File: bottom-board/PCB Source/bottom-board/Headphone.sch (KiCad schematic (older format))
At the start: 29 parts, among them P14 AudioJack3, Q10 MMBFJ110, Q9 MMBFJ110, U8 LM4811

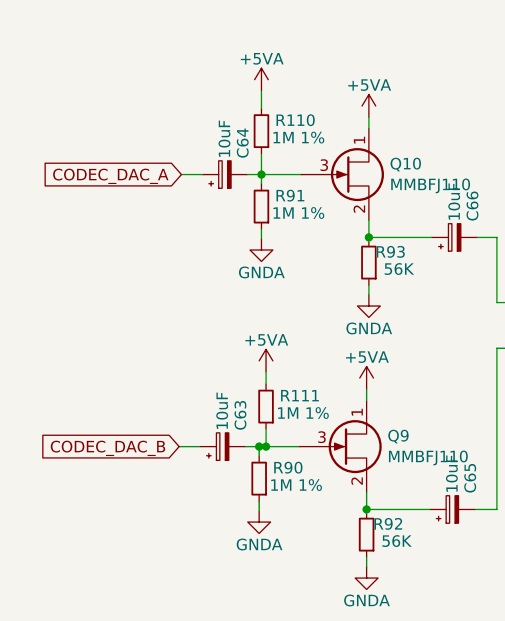
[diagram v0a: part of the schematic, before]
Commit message: update PCB, add noisefix components
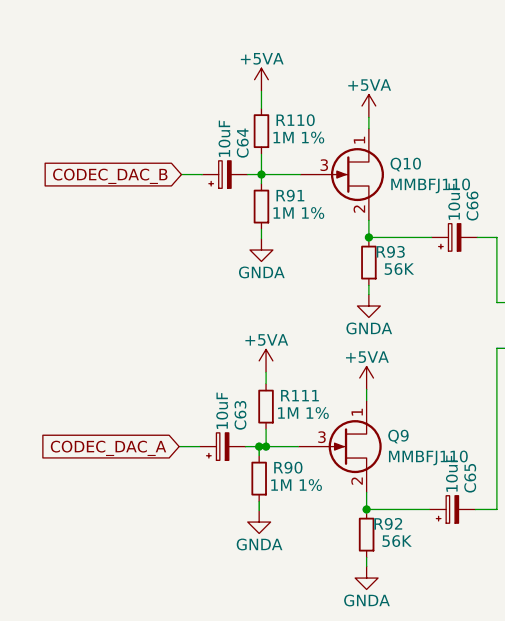
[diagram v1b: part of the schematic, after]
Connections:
- net CODEC_DAC_A: now also C63.1; no longer C64.1
- net CODEC_DAC_B: now also C64.1; no longer C63.1
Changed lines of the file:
@@
 Wire Wire Line
 	3965 2775 3965 2825
+Text GLabel 3145 3025 0    50   Input ~ 0
+CODEC_DAC_B
 Text GLabel 3135 4215 0    50   Input ~ 0
-CODEC_DAC_B
-Text GLabel 3145 3025 0    50   Input ~ 0
 CODEC_DAC_A
 Wire Wire Line

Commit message: update fabrication data
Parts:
- C67, C69: footprint Capacitor_SMD:C_0603_1608Metric -> Capacitor_SMD:C_0805_2012Metric; MPN EMK107BBJ106MA-T -> GRM219R61E106KA12D
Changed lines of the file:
@@
 F 0 "C67" H 6095 3080 50  0000 R CNN
 F 1 "10uF" H 5920 2930 50  0000 L CNN
-F 2 "Capacitor_SMD:C_0603_1608Metric" H 6135 3010 60  0001 C CNN
+F 2 "Capacitor_SMD:C_0805_2012Metric" H 6135 3010 60  0001 C CNN
 F 3 "" H 6135 3010 60  0000 C CNN
-F 4 "EMK107BBJ106MA-T" H 1685 1310 50  0001 C CNN "MPN"
+F 4 "GRM219R61E106KA12D" H 1685 1310 50  0001 C CNN "MPN"
 	1    6135 3010
 	1    0    0    -1
@@
 F 0 "C69" H 6255 4280 50  0000 R CNN
 F 1 "10uF" H 6080 4130 50  0000 L CNN
-F 2 "Capacitor_SMD:C_0603_1608Metric" H 6295 4210 60  0001 C CNN
+F 2 "Capacitor_SMD:C_0805_2012Metric" H 6295 4210 60  0001 C CNN
 F 3 "" H 6295 4210 60  0000 C CNN
-F 4 "EMK107BBJ106MA-T" H 1845 2510 50  0001 C CNN "MPN"
+F 4 "GRM219R61E106KA12D" H 1845 2510 50  0001 C CNN "MPN"
 	1    6295 4210
 	1    0    0    -1

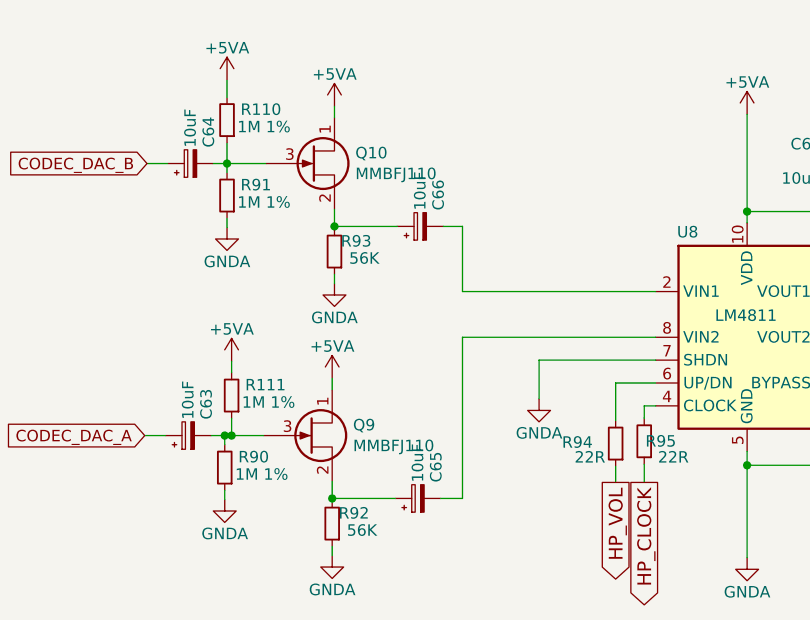
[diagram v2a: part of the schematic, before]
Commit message: change input bias 5->6V, reduce harmonics
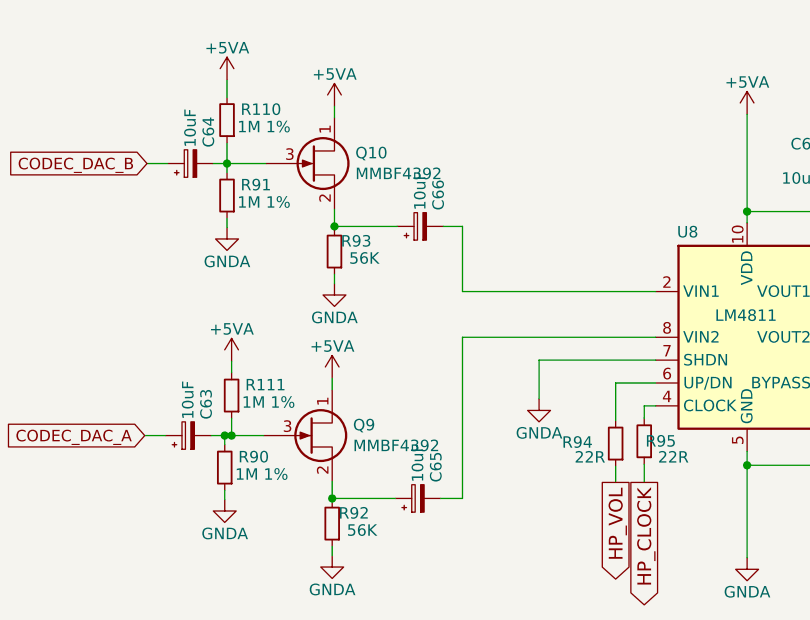
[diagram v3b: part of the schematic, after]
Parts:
- C70, C71: MPN UWX1C101MCL1GB -> 107SML016M
- Q10, Q9: value MMBFJ110 -> MMBF4392; MPN MMBFJ110 -> MMBF4392LT1G
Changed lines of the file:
@@
 AR Path="/5F5FD115/5F89CBDC" Ref="Q10"  Part="1"
 F 0 "Q10" H 4056 3071 50  0000 L CNN
-F 1 "MMBFJ110" H 4056 2980 50  0000 L CNN
+F 1 "MMBF4392" H 4056 2980 50  0000 L CNN
 F 2 "Package_TO_SOT_SMD:SOT-23" H 4065 3125 50  0001 C CNN
 F 3 "" H 3865 3025 50  0001 C CNN
-F 4 "MMBFJ110" H 3865 3025 50  0001 C CNN "MPN"
+F 4 "MMBF4392LT1G" H 3865 3025 50  0001 C CNN "MPN"
 	1    3865 3025
 	1    0    0    -1
@@
 AR Path="/5F5FD115/5F8D33CC" Ref="Q9"  Part="1"
 F 0 "Q9" H 4046 4261 50  0000 L CNN
-F 1 "MMBFJ110" H 4046 4170 50  0000 L CNN
+F 1 "MMBF4392" H 4046 4170 50  0000 L CNN
 F 2 "Package_TO_SOT_SMD:SOT-23" H 4055 4315 50  0001 C CNN
 F 3 "" H 3855 4215 50  0001 C CNN
-F 4 "MMBFJ110" H 3855 4215 50  0001 C CNN "MPN"
+F 4 "MMBF4392LT1G" H 3855 4215 50  0001 C CNN "MPN"
 	1    3855 4215
 	1    0    0    -1
@@
 F 2 "Capacitor_SMD:CP_Elec_6.3x7.7" H 6923 3365 30  0001 C CNN
 F 3 "" H 6885 3515 60  0000 C CNN
-F 4 "UWX1C101MCL1GB" H 3385 715 50  0001 C CNN "MPN"
+F 4 "107SML016M" H 3385 715 50  0001 C CNN "MPN"
 	1    6885 3515
 	0    -1   -1   0
@@
 F 2 "Capacitor_SMD:CP_Elec_6.3x7.7" H 6933 3790 30  0001 C CNN
 F 3 "" H 6895 3940 60  0000 C CNN
-F 4 "UWX1C101MCL1GB" H 3395 1140 50  0001 C CNN "MPN"
+F 4 "107SML016M" H 3395 1140 50  0001 C CNN "MPN"
 	1    6895 3940
 	0    -1   -1   0

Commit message: change JFET MPN
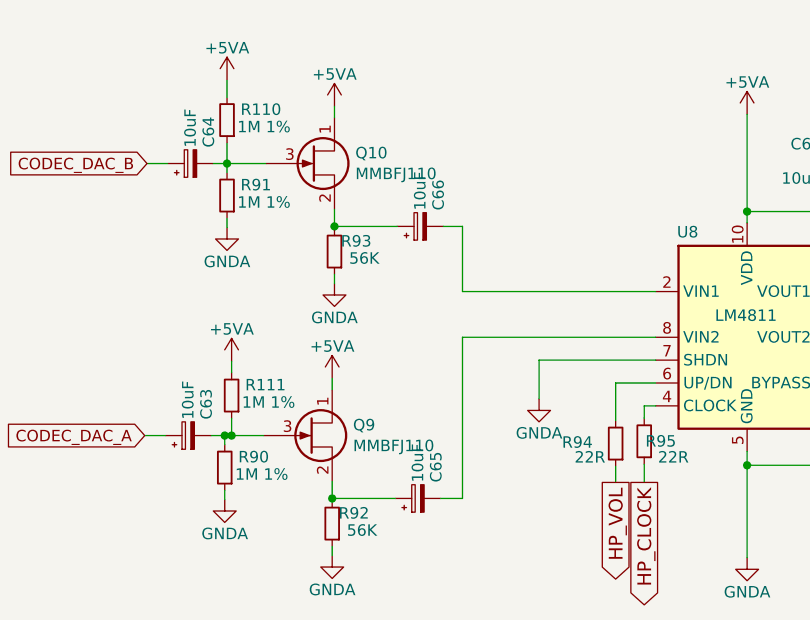
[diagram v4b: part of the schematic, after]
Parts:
- Q10, Q9: value MMBF4392 -> MMBFJ110; MPN MMBF4392LT1G -> MMBFJ110
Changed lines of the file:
@@
 AR Path="/5F5FD115/5F89CBDC" Ref="Q10"  Part="1"
 F 0 "Q10" H 4056 3071 50  0000 L CNN
-F 1 "MMBF4392" H 4056 2980 50  0000 L CNN
+F 1 "MMBFJ110" H 4056 2980 50  0000 L CNN
 F 2 "Package_TO_SOT_SMD:SOT-23" H 4065 3125 50  0001 C CNN
 F 3 "" H 3865 3025 50  0001 C CNN
-F 4 "MMBF4392LT1G" H 3865 3025 50  0001 C CNN "MPN"
+F 4 "MMBFJ110" H 3865 3025 50  0001 C CNN "MPN"
 	1    3865 3025
 	1    0    0    -1
@@
 AR Path="/5F5FD115/5F8D33CC" Ref="Q9"  Part="1"
 F 0 "Q9" H 4046 4261 50  0000 L CNN
-F 1 "MMBF4392" H 4046 4170 50  0000 L CNN
+F 1 "MMBFJ110" H 4046 4170 50  0000 L CNN
 F 2 "Package_TO_SOT_SMD:SOT-23" H 4055 4315 50  0001 C CNN
 F 3 "" H 3855 4215 50  0001 C CNN
-F 4 "MMBF4392LT1G" H 3855 4215 50  0001 C CNN "MPN"
+F 4 "MMBFJ110" H 3855 4215 50  0001 C CNN "MPN"
 	1    3855 4215
 	1    0    0    -1
